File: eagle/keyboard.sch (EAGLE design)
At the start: 71 parts, among them Q1 12MHz

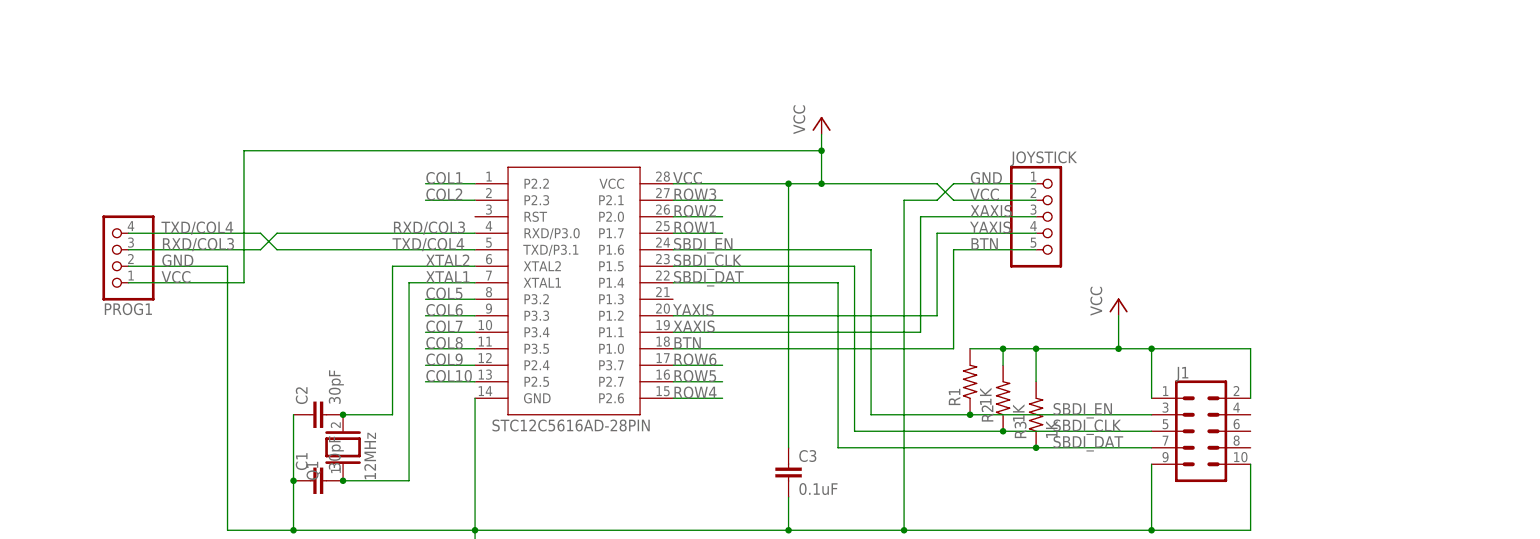
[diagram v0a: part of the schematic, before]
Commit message: Fix up schematic and finish placing the buttons in the keyboard brd
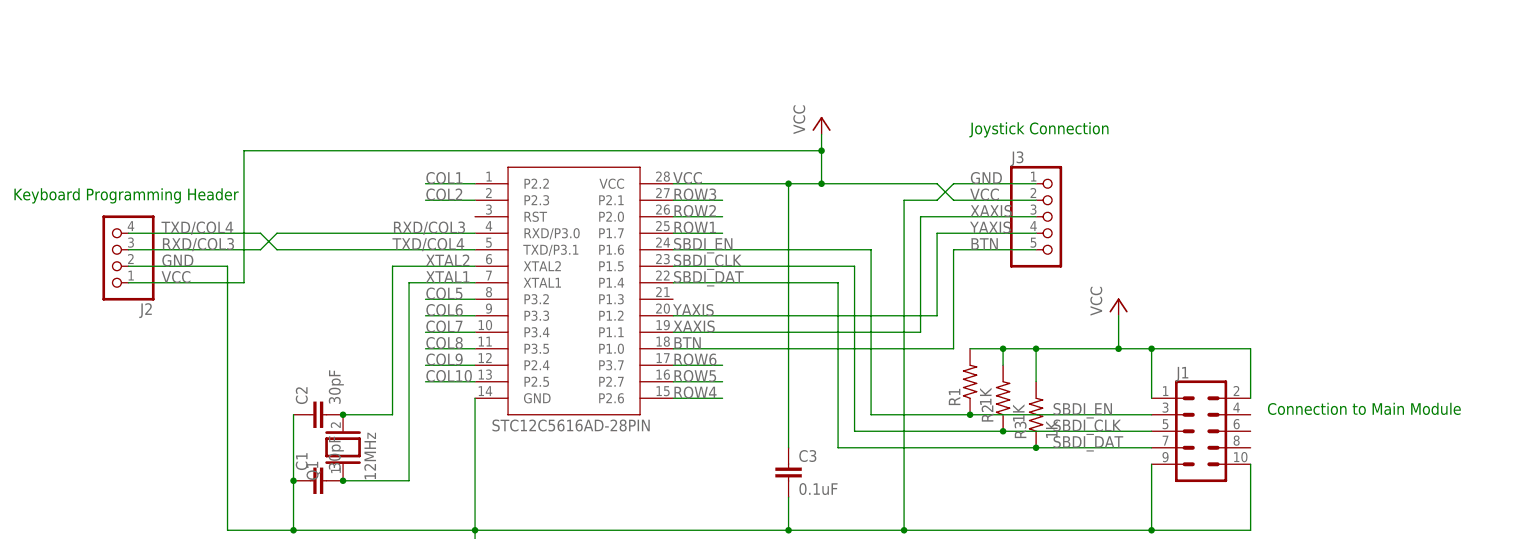
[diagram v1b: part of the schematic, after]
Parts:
- removed JOYSTICK: (no value), pinhead:PINHD-1X55X2MM
- added J3: (no value), pinhead:PINHD-1X5
- renumbered PROG1 to J2
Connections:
- net BTN: now also J3.5; no longer JOYSTICK.5
- net GND: now also J3.1; no longer JOYSTICK.1
- net VCC: now also J3.2; no longer JOYSTICK.2
- net XAXIS: now also J3.3; no longer JOYSTICK.3
- net YAXIS: now also J3.4; no longer JOYSTICK.4
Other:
- note added: "Connection to Main Module"
- note added: "Joystick Connection"
- note added: "Keyboard Programming Header"
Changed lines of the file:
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@@
 <part name="S60" library="switch-omron" library_urn="urn:adsk.eagle:library:377" deviceset="10-XX" device="" package3d_urn="urn:adsk.eagle:package:27496/1"/>
 <part name="U$1" library="TCalc" deviceset="STC12C5616AD-28PIN" device="" package3d_urn="urn:adsk.eagle:package:6673337/1"/>
-<part name="JOYSTICK" library="pinhead" library_urn="urn:adsk.eagle:library:325" deviceset="PINHD-1X5" device="5X2MM" package3d_urn="urn:adsk.eagle:package:22466/2"/>
+<part name="J3" library="pinhead" library_urn="urn:adsk.eagle:library:325" deviceset="PINHD-1X5" device="" package3d_urn="urn:adsk.eagle:package:22469/2"/>
 <part name="GND1" library="supply1" library_urn="urn:adsk.eagle:library:371" deviceset="GND" device=""/>
 <part name="Q1" library="special" library_urn="urn:adsk.eagle:library:367" deviceset="XTAL/S" device="" package3d_urn="urn:adsk.eagle:package:26647/2" value="12MHz"/>
@@
 <part name="C2" library="rcl" library_urn="urn:adsk.eagle:library:334" deviceset="C-EU" device="025-025X050" package3d_urn="urn:adsk.eagle:package:23629/2" value="30pF"/>
 <part name="P+1" library="supply1" library_urn="urn:adsk.eagle:library:371" deviceset="VCC" device=""/>
-<part name="PROG1" library="pinhead" library_urn="urn:adsk.eagle:library:325" deviceset="PINHD-1X4" device="" package3d_urn="urn:adsk.eagle:package:22407/2"/>
+<part name="J2" library="pinhead" library_urn="urn:adsk.eagle:library:325" deviceset="PINHD-1X4" device="" package3d_urn="urn:adsk.eagle:package:22407/2"/>
 <part name="P+2" library="supply1" library_urn="urn:adsk.eagle:library:371" deviceset="VCC" device=""/>
 <part name="R1" library="rcl" library_urn="urn:adsk.eagle:library:334" deviceset="R-US_" device="0204/7" package3d_urn="urn:adsk.eagle:package:23498/1" value="1K"/>
@@
 <sheet>
 <plain>
+<text x="22.86" y="76.2" size="1.778" layer="91">Keyboard Programming Header</text>
+<text x="170.18" y="86.36" size="1.778" layer="91">Joystick Connection</text>
+<text x="215.9" y="43.18" size="1.778" layer="91">Connection to Main Module</text>
 </plain>
 <instances>
@@
 </instance>
 <instance part="U$1" gate="G$1" x="109.22" y="58.42" smashed="yes"/>
-<instance part="JOYSTICK" gate="A" x="182.88" y="73.66" smashed="yes">
+<instance part="J3" gate="A" x="182.88" y="73.66" smashed="yes">
 <attribute name="NAME" x="176.53" y="81.915" size="1.778" layer="95"/>
 <attribute name="VALUE" x="176.53" y="63.5" size="1.778" layer="96"/>
@@
 <attribute name="VALUE" x="144.78" y="86.36" size="1.778" layer="96" rot="R90"/>
 </instance>
-<instance part="PROG1" gate="A" x="38.1" y="68.58" smashed="yes" rot="R180">
+<instance part="J2" gate="A" x="38.1" y="68.58" smashed="yes" rot="R180">
 <attribute name="NAME" x="44.45" y="60.325" size="1.778" layer="95" rot="R180"/>
 <attribute name="VALUE" x="44.45" y="76.2" size="1.778" layer="96" rot="R180"/>
@@
 <wire x1="66.04" y1="25.4" x2="93.98" y2="25.4" width="0.1524" layer="91"/>
 <junction x="66.04" y="33.02"/>
-<pinref part="PROG1" gate="A" pin="2"/>
+<pinref part="J2" gate="A" pin="2"/>
 <wire x1="40.64" y1="66.04" x2="55.88" y2="66.04" width="0.1524" layer="91"/>
 <wire x1="55.88" y1="66.04" x2="55.88" y2="25.4" width="0.1524" layer="91"/>
@@
 <label x="45.72" y="66.04" size="1.778" layer="95"/>
 <wire x1="160.02" y1="76.2" x2="165.1" y2="76.2" width="0.1524" layer="91"/>
-<pinref part="JOYSTICK" gate="A" pin="1"/>
+<pinref part="J3" gate="A" pin="1"/>
 <wire x1="165.1" y1="76.2" x2="167.64" y2="78.74" width="0.1524" layer="91"/>
 <wire x1="167.64" y1="78.74" x2="180.34" y2="78.74" width="0.1524" layer="91"/>
@@
 <net name="XAXIS" class="0">
 <segment>
-<pinref part="JOYSTICK" gate="A" pin="3"/>
+<pinref part="J3" gate="A" pin="3"/>
 <wire x1="180.34" y1="73.66" x2="162.56" y2="73.66" width="0.1524" layer="91"/>
 <label x="170.18" y="73.66" size="1.778" layer="95"/>
@@
 <net name="YAXIS" class="0">
 <segment>
-<pinref part="JOYSTICK" gate="A" pin="4"/>
+<pinref part="J3" gate="A" pin="4"/>
 <wire x1="180.34" y1="71.12" x2="165.1" y2="71.12" width="0.1524" layer="91"/>
 <label x="170.18" y="71.12" size="1.778" layer="95"/>
@@
 <net name="BTN" class="0">
 <segment>
-<pinref part="JOYSTICK" gate="A" pin="5"/>
+<pinref part="J3" gate="A" pin="5"/>
 <wire x1="180.34" y1="68.58" x2="167.64" y2="68.58" width="0.1524" layer="91"/>
 <wire x1="167.64" y1="68.58" x2="167.64" y2="53.34" width="0.1524" layer="91"/>
@@
 <wire x1="142.24" y1="78.74" x2="124.46" y2="78.74" width="0.1524" layer="91"/>
 <wire x1="147.32" y1="86.36" x2="147.32" y2="83.82" width="0.1524" layer="91"/>
-<pinref part="PROG1" gate="A" pin="1"/>
+<pinref part="J2" gate="A" pin="1"/>
 <wire x1="147.32" y1="83.82" x2="147.32" y2="78.74" width="0.1524" layer="91"/>
 <wire x1="40.64" y1="63.5" x2="58.42" y2="63.5" width="0.1524" layer="91"/>
@@
 <wire x1="147.32" y1="78.74" x2="165.1" y2="78.74" width="0.1524" layer="91"/>
 <junction x="147.32" y="78.74"/>
-<pinref part="JOYSTICK" gate="A" pin="2"/>
+<pinref part="J3" gate="A" pin="2"/>
 <wire x1="165.1" y1="78.74" x2="167.64" y2="76.2" width="0.1524" layer="91"/>
 <wire x1="167.64" y1="76.2" x2="180.34" y2="76.2" width="0.1524" layer="91"/>
@@
 <wire x1="63.5" y1="71.12" x2="93.98" y2="71.12" width="0.1524" layer="91"/>
 <label x="81.28" y="71.12" size="1.778" layer="95"/>
-<pinref part="PROG1" gate="A" pin="3"/>
+<pinref part="J2" gate="A" pin="3"/>
 <wire x1="40.64" y1="68.58" x2="60.96" y2="68.58" width="0.1524" layer="91"/>
 <wire x1="60.96" y1="68.58" x2="63.5" y2="71.12" width="0.1524" layer="91"/>
@@
 <wire x1="63.5" y1="68.58" x2="93.98" y2="68.58" width="0.1524" layer="91"/>
 <label x="81.28" y="68.58" size="1.778" layer="95"/>
-<pinref part="PROG1" gate="A" pin="4"/>
+<pinref part="J2" gate="A" pin="4"/>
 <wire x1="40.64" y1="71.12" x2="60.96" y2="71.12" width="0.1524" layer="91"/>
 <wire x1="60.96" y1="71.12" x2="63.5" y2="68.58" width="0.1524" layer="91"/>

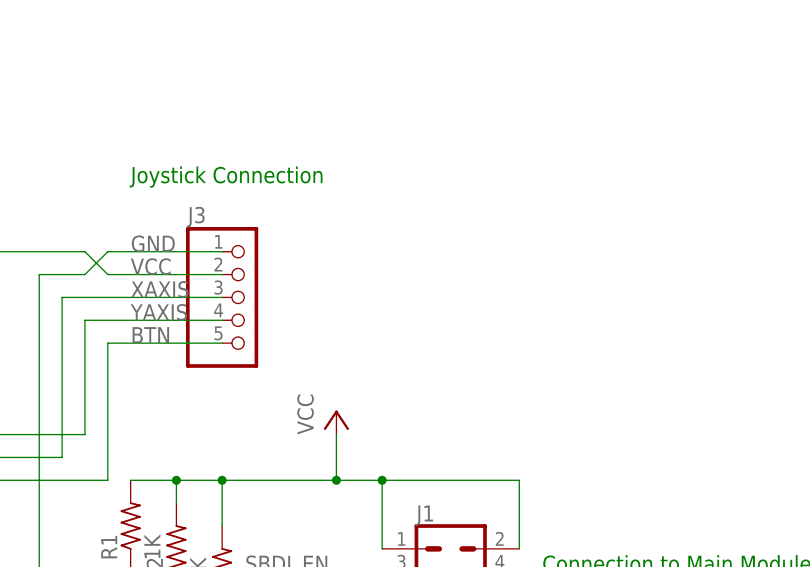
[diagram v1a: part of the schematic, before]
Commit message: Add joystick support in keyboard schematic
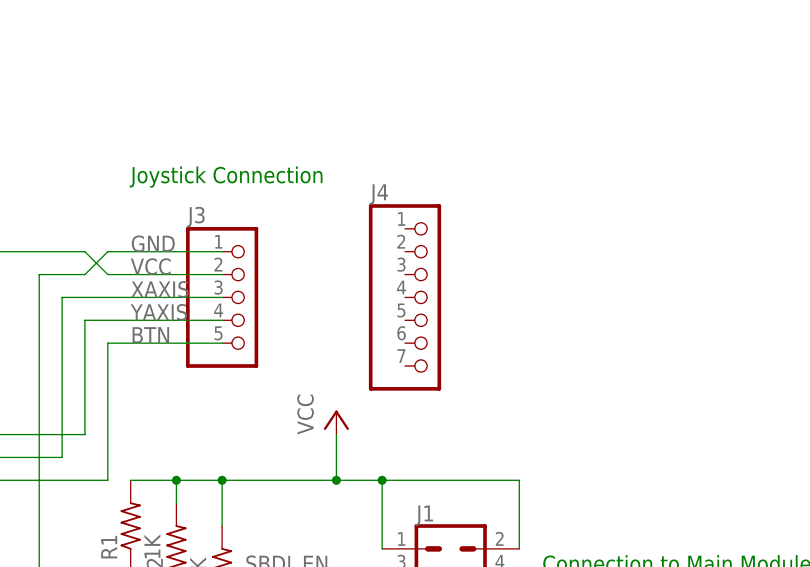
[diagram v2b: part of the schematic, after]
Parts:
- added J4: (no value), pinhead:PINHD-1X7
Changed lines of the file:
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@@
 <part name="J1" library="SparkFun-Connectors" library_urn="urn:adsk.eagle:library:513" deviceset="CONN_05X2" device="SHD_LOCK" package3d_urn="urn:adsk.eagle:package:38007/1"/>
 <part name="C3" library="rcl" library_urn="urn:adsk.eagle:library:334" deviceset="C-EU" device="025-030X050" package3d_urn="urn:adsk.eagle:package:23631/1" value="0.1uF"/>
+<part name="J4" library="pinhead" library_urn="urn:adsk.eagle:library:325" deviceset="PINHD-1X7" device="" package3d_urn="urn:adsk.eagle:package:22477/2"/>
 </parts>
 <sheets>
@@
 <attribute name="VALUE" x="143.764" y="30.861" size="1.778" layer="96"/>
 </instance>
+<instance part="J4" gate="A" x="203.2" y="73.66" smashed="yes">
+<attribute name="NAME" x="196.85" y="84.455" size="1.778" layer="95"/>
+<attribute name="VALUE" x="196.85" y="60.96" size="1.778" layer="96"/>
+</instance>
 </instances>

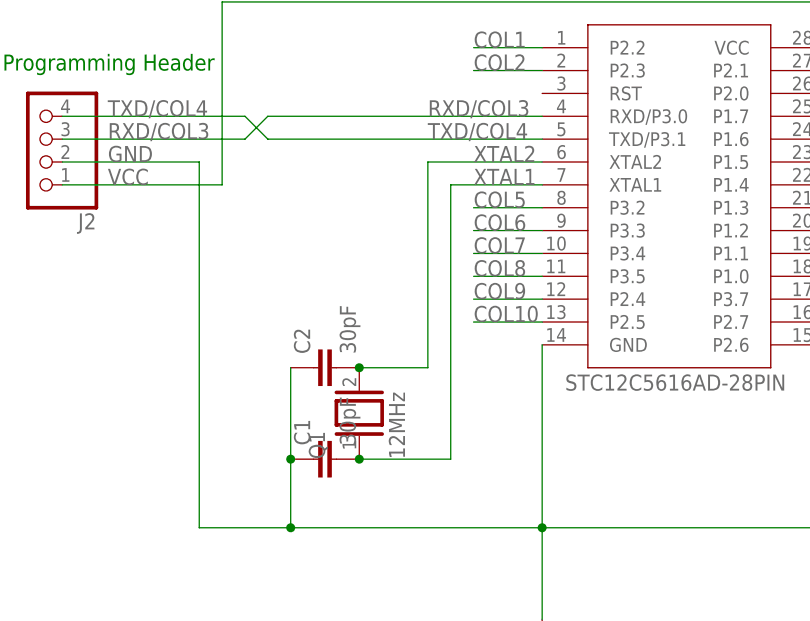
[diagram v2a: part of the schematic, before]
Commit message: Finish placing components
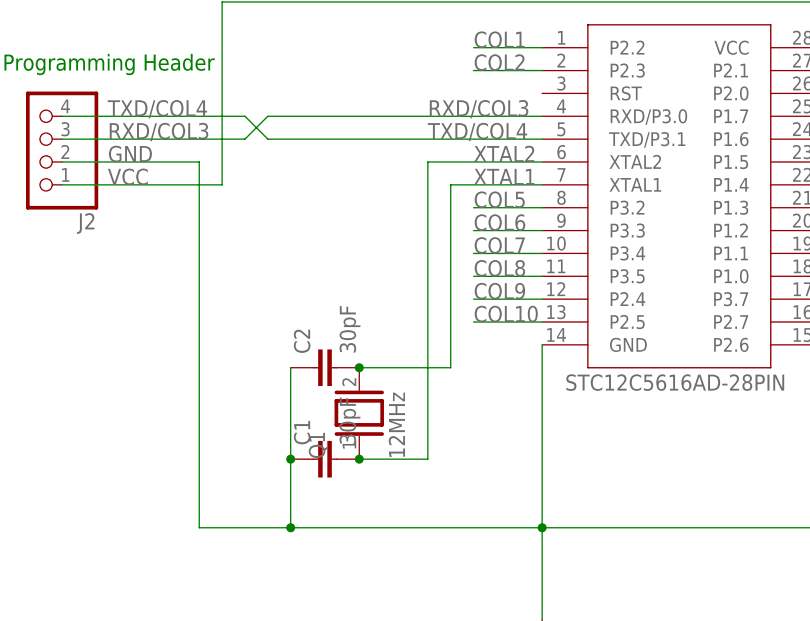
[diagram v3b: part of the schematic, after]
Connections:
- net XTAL1: now also C2.2, Q1.2; no longer C1.2, Q1.1
- net XTAL2: now also C1.2, Q1.1; no longer C2.2, Q1.2
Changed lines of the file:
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@@
 <pinref part="U$1" gate="G$1" pin="XTAL2"/>
 <wire x1="93.98" y1="66.04" x2="81.28" y2="66.04" width="0.1524" layer="91"/>
-<wire x1="81.28" y1="66.04" x2="81.28" y2="43.18" width="0.1524" layer="91"/>
-<pinref part="Q1" gate="G$1" pin="2"/>
-<wire x1="81.28" y1="43.18" x2="73.66" y2="43.18" width="0.1524" layer="91"/>
-<pinref part="C2" gate="G$1" pin="2"/>
-<junction x="73.66" y="43.18"/>
 <label x="86.36" y="66.04" size="1.778" layer="95"/>
+<pinref part="Q1" gate="G$1" pin="1"/>
+<pinref part="C1" gate="G$1" pin="2"/>
+<wire x1="73.66" y1="33.02" x2="81.28" y2="33.02" width="0.1524" layer="91"/>
+<wire x1="81.28" y1="33.02" x2="81.28" y2="66.04" width="0.1524" layer="91"/>
+<junction x="73.66" y="33.02"/>
 </segment>
 </net>
 <net name="XTAL1" class="0">
 <segment>
-<pinref part="Q1" gate="G$1" pin="1"/>
 <pinref part="U$1" gate="G$1" pin="XTAL1"/>
-<pinref part="C1" gate="G$1" pin="2"/>
-<junction x="73.66" y="33.02"/>
 <label x="86.36" y="63.5" size="1.778" layer="95"/>
-<wire x1="73.66" y1="33.02" x2="83.82" y2="33.02" width="0.1524" layer="91"/>
-<wire x1="83.82" y1="33.02" x2="83.82" y2="63.5" width="0.1524" layer="91"/>
 <wire x1="83.82" y1="63.5" x2="93.98" y2="63.5" width="0.1524" layer="91"/>
+<pinref part="Q1" gate="G$1" pin="2"/>
+<pinref part="C2" gate="G$1" pin="2"/>
+<wire x1="73.66" y1="43.18" x2="83.82" y2="43.18" width="0.1524" layer="91"/>
+<wire x1="83.82" y1="43.18" x2="83.82" y2="63.5" width="0.1524" layer="91"/>
+<junction x="73.66" y="43.18"/>
 </segment>
 </net>
